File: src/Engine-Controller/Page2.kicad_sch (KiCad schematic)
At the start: 25 parts, among them P2 Solid Prop Cont, P4 Micro_SD_Card, P5 USB, P6 140-504-415-000, U11 TS391IYLT, U4 SST25VF040B-50-4I-S2AE-T, U5 CP2102-GMR(QFN28)

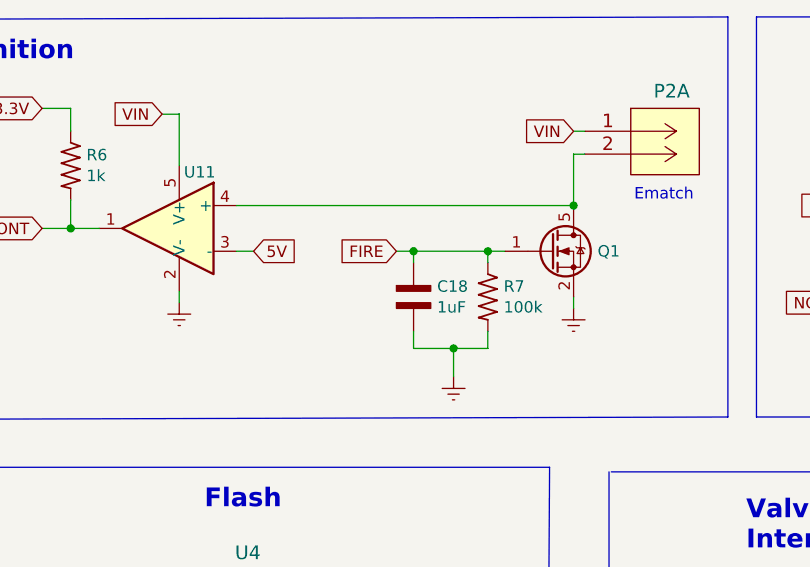
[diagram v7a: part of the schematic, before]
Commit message: added thermocouple IC to lib files
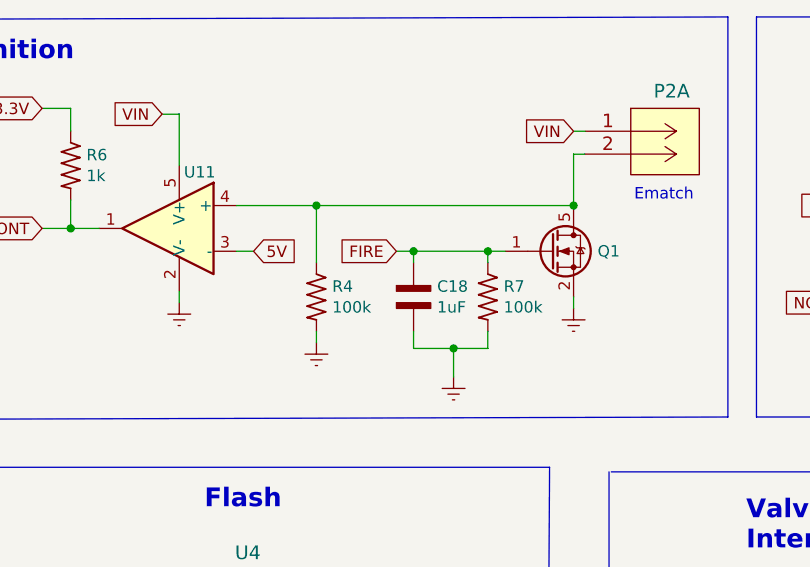
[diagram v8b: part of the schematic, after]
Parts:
- added R4: 100k, Engine-Controller:RES_0603, symbol Engine-Controller:RES_0603
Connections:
- net Earth: now also R4.2
- net at P2.2 (6), Q1.5 (D), U11.4 (+): now also R4.1
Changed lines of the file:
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@@
   (junction (at 78.74 138.43) (diameter 0) (color 0 0 0 0)
+  )
+  (junction (at 63.5 122.555) (diameter 0) (color 0 0 0 0)
   )
   (junction (at 92.075 122.555) (diameter 0) (color 0 0 0 0)
@@
     (stroke (width 0) (type default) (color 0 0 0 0))
   )
+  (wire (pts (xy 63.5 136.525) (xy 63.5 137.795))
+    (stroke (width 0) (type default) (color 0 0 0 0))
+  )
   (wire (pts (xy 69.215 165.735) (xy 71.12 165.735))
     (stroke (width 0) (type default) (color 0 0 0 0))
@@
     (stroke (width 0) (type default) (color 0 0 0 0))
   )
+  (wire (pts (xy 63.5 122.555) (xy 63.5 128.905))
+    (stroke (width 0) (type default) (color 0 0 0 0))
+  )
   (wire (pts (xy 86.36 72.39) (xy 86.36 73.914))
     (stroke (width 0) (type default) (color 0 0 0 0))
@@
     (stroke (width 0) (type default) (color 0 0 0 0))
   )
-  (wire (pts (xy 54.61 122.555) (xy 92.075 122.555))
+  (wire (pts (xy 54.61 122.555) (xy 63.5 122.555))
     (stroke (width 0) (type default) (color 0 0 0 0))
   )
@@
   )
   (wire (pts (xy 42.545 173.355) (xy 40.64 173.355))
+    (stroke (width 0) (type default) (color 0 0 0 0))
+  )
+  (wire (pts (xy 63.5 122.555) (xy 92.075 122.555))
     (stroke (width 0) (type default) (color 0 0 0 0))
   )
@@
     (pin "1")
   )
+  (symbol (lib_id "Engine-Controller:RES_0603") (at 63.5 132.715 270) (unit 1)
+    (in_bom yes) (on_board yes)
+    (property "Reference" "R4" (id 0) (at 65.2526 131.5466 90)
+      (effects (font (size 1.27 1.27)) (justify left))
+    )
+    (property "Value" "100k" (id 1) (at 65.2526 133.858 90)
+      (effects (font (size 1.27 1.27)) (justify left))
+    )
+    (property "Footprint" "Engine-Controller:RES_0603" (id 2) (at 50.8 133.985 0)
+      (effects (font (size 1.27 1.27)) (justify left bottom) hide)
+    )
+    (property "Datasheet" "" (id 3) (at 63.5 132.715 0)
+      (effects (font (size 1.27 1.27)) (justify left bottom) hide)
+    )
+    (pin "1")
+    (pin "2")
+  )
   (symbol (lib_id "Engine-Controller:RES_0603") (at 82.55 132.715 270) (unit 1)
     (in_bom yes) (on_board yes)
@@
       (effects (font (size 1.27 1.27)) hide)
     )
+    (pin "1")
+  )
+  (symbol (lib_id "Engine-Controller:Earth") (at 63.5 137.795 0) (unit 1)
+    (in_bom yes) (on_board yes)
+    (property "Reference" "#PWR034" (id 0) (at 63.5 144.145 0)
+      (effects (font (size 1.27 1.27)) hide)
+    )
+    (property "Value" "Earth" (id 1) (at 63.5 141.605 0)
+      (effects (font (size 1.27 1.27)) hide)
+    )
+    (property "Footprint" "" (id 2) (at 63.5 137.795 0)
+      (effects (font (size 1.27 1.27)) hide)
+    )
+    (property "Datasheet" "" (id 3) (at 63.5 137.795 0)
+      (effects (font (size 1.27 1.27)) hide)
+    )
